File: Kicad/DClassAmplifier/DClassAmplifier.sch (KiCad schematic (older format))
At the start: 9 parts

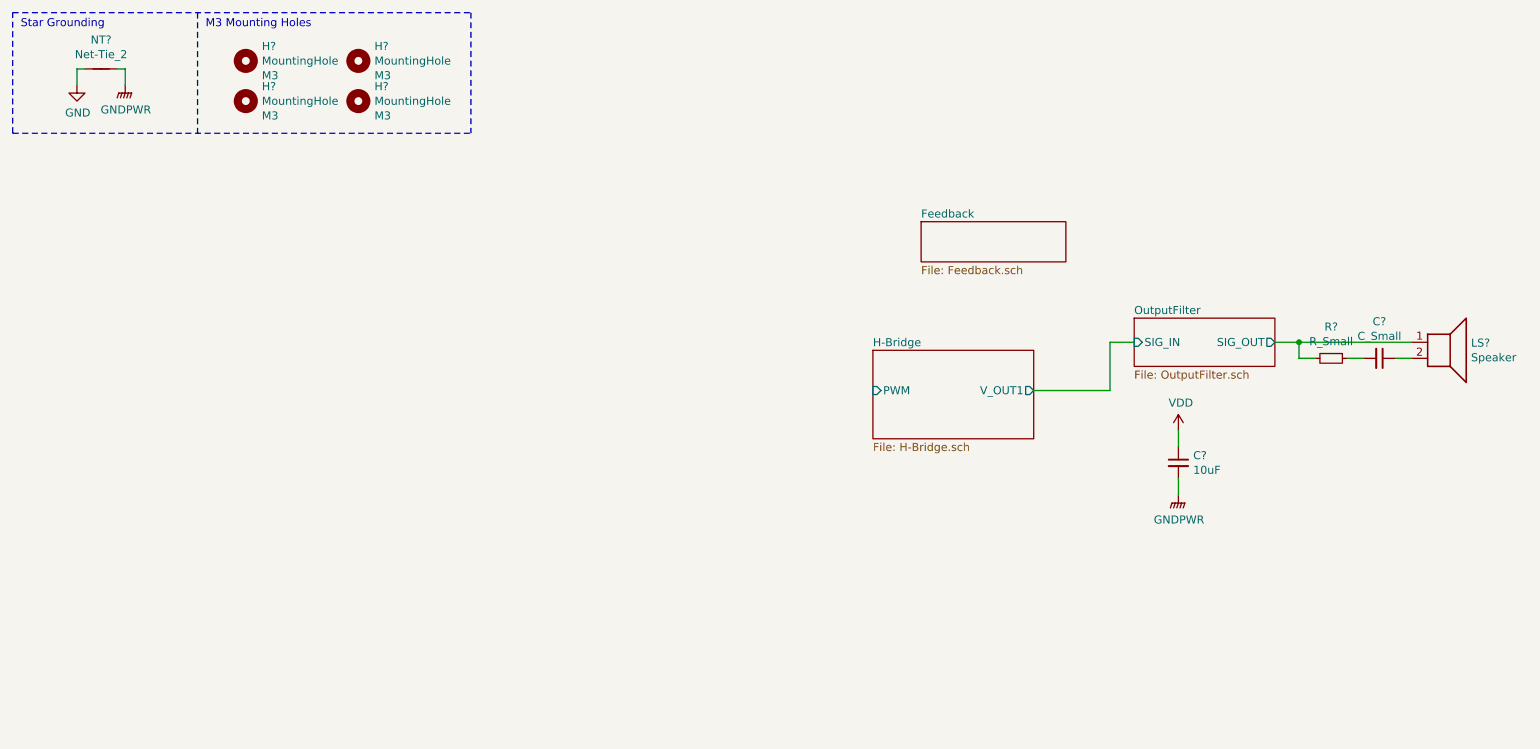
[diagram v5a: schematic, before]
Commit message: Added Dummy Comparator to schematic and duplicated drive.
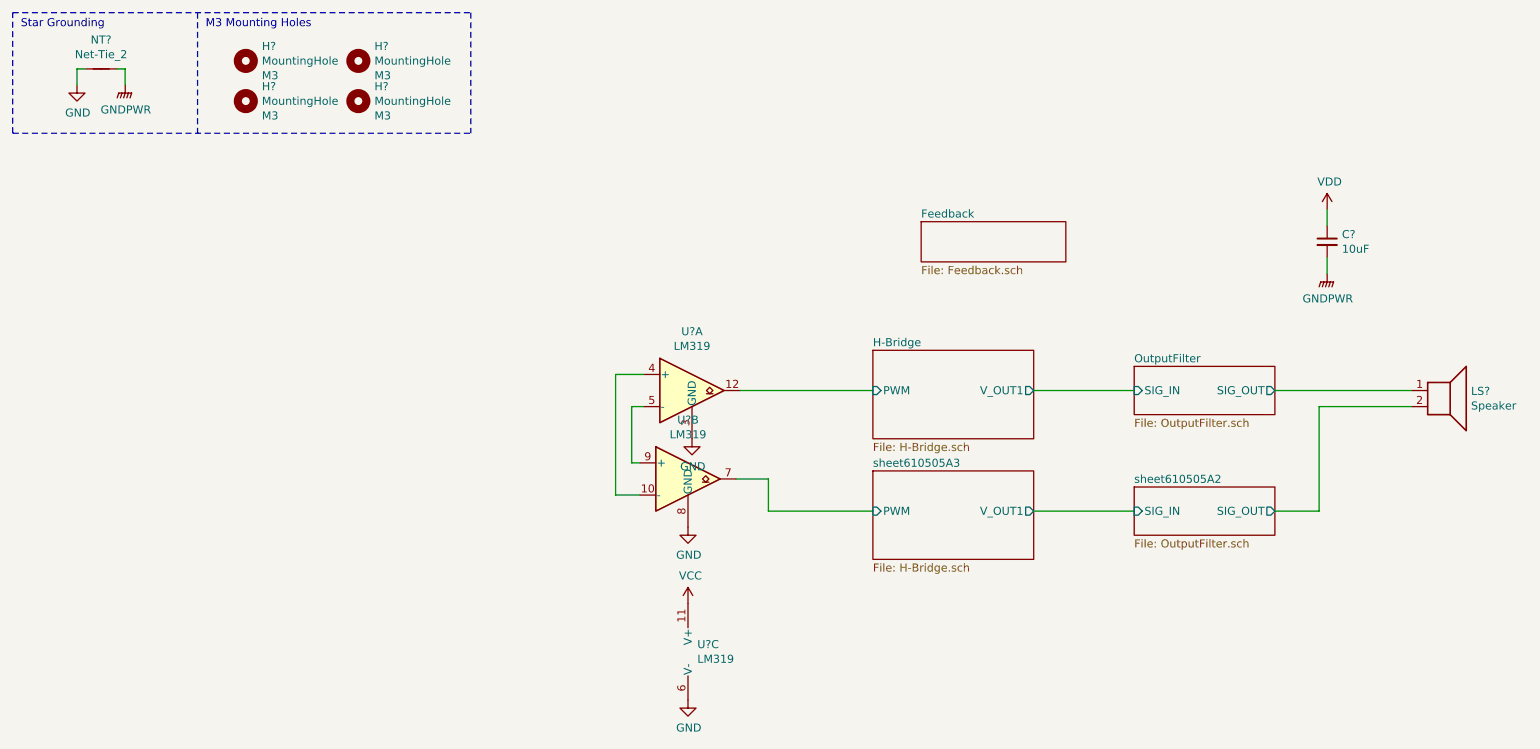
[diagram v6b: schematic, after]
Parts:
- removed C?: C_Small, symbol Device:C_Small
- removed R?: R_Small, symbol Device:R_Small
- added U? (x3): LM319, symbol Comparator:LM319
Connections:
- net GND: now also U?.3 (GND), U?.6 (V-), U?.8 (GND)
- net H-Bridge/PWM: now also U?.12
- net sheet610505A2/SIG_OUT: now reaches LS?.2
- new net: U?.10 (-), U?.4 (+)
- new net: U?.5 (-), U?.9 (+)
- new net VCC: U?.11 (V+)
- new net sheet610505A3/PWM: U?.7
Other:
- moved on the sheet: C?, LS?
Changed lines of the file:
@@
 $Descr A4 11693 8268
 encoding utf-8
-Sheet 1 4
+Sheet 1 6
 Title ""
 Date ""
@@
 $EndDescr
 $Sheet
-S 7625 2500 875  300
+S 7625 2800 875  300
 U 60F78807
 F0 "OutputFilter" 50
 F1 "OutputFilter.sch" 50
-F2 "SIG_IN" I L 7625 2650 50
-F3 "SIG_OUT" O R 8500 2650 50
+F2 "SIG_IN" I L 7625 2950 50
+F3 "SIG_OUT" O R 8500 2950 50
 $EndSheet
 $Comp
@@
 L Device:Speaker LS?
 U 1 1 60FD7EA0
-P 9550 2650
-F 0 "LS?" H 9720 2646 50  0000 L CNN
-F 1 "Speaker" H 9720 2555 50  0000 L CNN
-F 2 "" H 9550 2450 50  0001 C CNN
-F 3 "~" H 9540 2600 50  0001 C CNN
-	1    9550 2650
-	1    0    0    -1
-$EndComp
-Wire Wire Line
-	9350 2650 8650 2650
-$Comp
-L Device:R_Small R?
-U 1 1 60FD8CE8
-P 8850 2750
-F 0 "R?" V 8654 2750 50  0000 C CNN
-F 1 "R_Small" V 8745 2750 50  0000 C CNN
-F 2 "" H 8850 2750 50  0001 C CNN
-F 3 "~" H 8850 2750 50  0001 C CNN
-	1    8850 2750
-	0    1    1    0
-$EndComp
-$Comp
-L Device:C_Small C?
-U 1 1 60FD982C
-P 9150 2750
-F 0 "C?" V 8921 2750 50  0000 C CNN
-F 1 "C_Small" V 9012 2750 50  0000 C CNN
-F 2 "" H 9150 2750 50  0001 C CNN
-F 3 "~" H 9150 2750 50  0001 C CNN
-	1    9150 2750
-	0    1    1    0
-$EndComp
-Wire Wire Line
-	9250 2750 9350 2750
-Wire Wire Line
-	9050 2750 8950 2750
-Wire Wire Line
-	8750 2750 8650 2750
-Wire Wire Line
-	8650 2750 8650 2650
-Connection ~ 8650 2650
-Wire Wire Line
-	8650 2650 8500 2650
+P 9550 2950
+F 0 "LS?" H 9720 2946 50  0000 L CNN
+F 1 "Speaker" H 9720 2855 50  0000 L CNN
+F 2 "" H 9550 2750 50  0001 C CNN
+F 3 "~" H 9540 2900 50  0001 C CNN
+	1    9550 2950
+	1    0    0    -1
+$EndComp
 $Sheet
 S 6300 1900 900  250
@@
 Text Notes 1850 700  0    50   ~ 0
 M3 Mounting Holes
-Wire Wire Line
-	7625 2650 7475 2650
-Wire Wire Line
-	7475 2650 7475 2950
-Wire Wire Line
-	7475 2950 7000 2950
 $Comp
 L power:VDD #PWR?
 U 1 1 6101A943
-P 7900 3200
-F 0 "#PWR?" H 7900 3050 50  0001 C CNN
-F 1 "VDD" H 7915 3373 50  0000 C CNN
-F 2 "" H 7900 3200 50  0001 C CNN
-F 3 "" H 7900 3200 50  0001 C CNN
-	1    7900 3200
+P 8825 1825
+F 0 "#PWR?" H 8825 1675 50  0001 C CNN
+F 1 "VDD" H 8840 1998 50  0000 C CNN
+F 2 "" H 8825 1825 50  0001 C CNN
+F 3 "" H 8825 1825 50  0001 C CNN
+	1    8825 1825
 	1    0    0    -1
 $EndComp
@@
 L power:GNDPWR #PWR?
 U 1 1 6101A949
-P 7900 3600
-F 0 "#PWR?" H 7900 3400 50  0001 C CNN
-F 1 "GNDPWR" H 7904 3446 50  0000 C CNN
-F 2 "" H 7900 3550 50  0001 C CNN
-F 3 "" H 7900 3550 50  0001 C CNN
-	1    7900 3600
+P 8825 2225
+F 0 "#PWR?" H 8825 2025 50  0001 C CNN
+F 1 "GNDPWR" H 8829 2071 50  0000 C CNN
+F 2 "" H 8825 2175 50  0001 C CNN
+F 3 "" H 8825 2175 50  0001 C CNN
+	1    8825 2225
 	1    0    0    -1
 $EndComp
@@
 L Device:C_Small C?
 U 1 1 6101A94F
-P 7900 3400
+P 8825 2025
 AR Path="/60FDBB90/6101A94F" Ref="C?"  Part="1"
 AR Path="/6101A94F" Ref="C?"  Part="1"
-F 0 "C?" H 7992 3446 50  0000 L CNN
-F 1 "10uF" H 7992 3355 50  0000 L CNN
-F 2 "" H 7900 3400 50  0001 C CNN
-F 3 "~" H 7900 3400 50  0001 C CNN
-	1    7900 3400
-	1    0    0    -1
-$EndComp
-Wire Wire Line
-	7900 3600 7900 3500
-Wire Wire Line
-	7900 3200 7900 3300
+F 0 "C?" H 8917 2071 50  0000 L CNN
+F 1 "10uF" H 8917 1980 50  0000 L CNN
+F 2 "" H 8825 2025 50  0001 C CNN
+F 3 "~" H 8825 2025 50  0001 C CNN
+	1    8825 2025
+	1    0    0    -1
+$EndComp
+Wire Wire Line
+	8825 2225 8825 2125
+Wire Wire Line
+	8825 1825 8825 1925
+$Comp
+L Comparator:LM319 U?
+U 1 1 6103E3C3
+P 4875 2950
+F 0 "U?" H 4875 3317 50  0000 C CNN
+F 1 "LM319" H 4875 3226 50  0000 C CNN
+F 2 "" H 4875 2950 50  0001 C CNN
+F 3 "http://www.ti.com/lit/ds/symlink/lm319-n.pdf" H 4875 2950 50  0001 C CNN
+	1    4875 2950
+	1    0    0    -1
+$EndComp
+$Comp
+L Comparator:LM319 U?
+U 2 1 6103EEF0
+P 4850 3500
+F 0 "U?" H 4850 3867 50  0000 C CNN
+F 1 "LM319" H 4850 3776 50  0000 C CNN
+F 2 "" H 4850 3500 50  0001 C CNN
+F 3 "http://www.ti.com/lit/ds/symlink/lm319-n.pdf" H 4850 3500 50  0001 C CNN
+	2    4850 3500
+	1    0    0    -1
+$EndComp
+$Comp
+L Comparator:LM319 U?
+U 3 1 6103FBAA
+P 4950 4575
+F 0 "U?" H 4908 4621 50  0000 L CNN
+F 1 "LM319" H 4908 4530 50  0000 L CNN
+F 2 "" H 4950 4575 50  0001 C CNN
+F 3 "http://www.ti.com/lit/ds/symlink/lm319-n.pdf" H 4950 4575 50  0001 C CNN
+	3    4950 4575
+	1    0    0    -1
+$EndComp
+Wire Wire Line
+	6000 2950 5175 2950
+Wire Wire Line
+	8500 2950 9350 2950
+Wire Wire Line
+	7000 2950 7625 2950
+$Sheet
+S 7625 3550 875  300
+U 610505A7
+F0 "sheet610505A2" 50
+F1 "OutputFilter.sch" 50
+F2 "SIG_IN" I L 7625 3700 50
+F3 "SIG_OUT" O R 8500 3700 50
+$EndSheet
+$Sheet
+S 6000 3450 1000 550
+U 610505AB
+F0 "sheet610505A3" 50
+F1 "H-Bridge.sch" 50
+F2 "PWM" I L 6000 3700 50
+F3 "V_OUT1" O R 7000 3700 50
+$EndSheet
+Wire Wire Line
+	7000 3700 7625 3700
+Wire Wire Line
+	8500 3700 8775 3700
+Wire Wire Line
+	8775 3700 8775 3050
+Wire Wire Line
+	8775 3050 9350 3050
+Wire Wire Line
+	6000 3700 5350 3700
+Wire Wire Line
+	5350 3700 5350 3500
+Wire Wire Line
+	5350 3500 5150 3500
+Wire Wire Line
+	4575 3050 4500 3050
+Wire Wire Line
+	4500 3050 4500 3400
+Wire Wire Line
+	4500 3400 4550 3400
+Wire Wire Line
+	4575 2850 4400 2850
+Wire Wire Line
+	4400 2850 4400 3600
+Wire Wire Line
+	4400 3600 4550 3600
+$Comp
+L power:GND #PWR?
+U 1 1 61053271
+P 4875 3250
+F 0 "#PWR?" H 4875 3000 50  0001 C CNN
+F 1 "GND" H 4880 3077 50  0000 C CNN
+F 2 "" H 4875 3250 50  0001 C CNN
+F 3 "" H 4875 3250 50  0001 C CNN
+	1    4875 3250
+	1    0    0    -1
+$EndComp
+$Comp
+L power:GND #PWR?
+U 1 1 61053814
+P 4850 3800
+F 0 "#PWR?" H 4850 3550 50  0001 C CNN
+F 1 "GND" H 4855 3627 50  0000 C CNN
+F 2 "" H 4850 3800 50  0001 C CNN
+F 3 "" H 4850 3800 50  0001 C CNN
+	1    4850 3800
+	1    0    0    -1
+$EndComp
+$Comp
+L power:GND #PWR?
+U 1 1 61054142
+P 4850 4875
+F 0 "#PWR?" H 4850 4625 50  0001 C CNN
+F 1 "GND" H 4855 4702 50  0000 C CNN
+F 2 "" H 4850 4875 50  0001 C CNN
+F 3 "" H 4850 4875 50  0001 C CNN
+	1    4850 4875
+	1    0    0    -1
+$EndComp
+$Comp
+L power:VCC #PWR?
+U 1 1 6105AFC3
+P 4850 4275
+F 0 "#PWR?" H 4850 4125 50  0001 C CNN
+F 1 "VCC" H 4865 4448 50  0000 C CNN
+F 2 "" H 4850 4275 50  0001 C CNN
+F 3 "" H 4850 4275 50  0001 C CNN
+	1    4850 4275
+	1    0    0    -1
+$EndComp
 $EndSCHEMATC

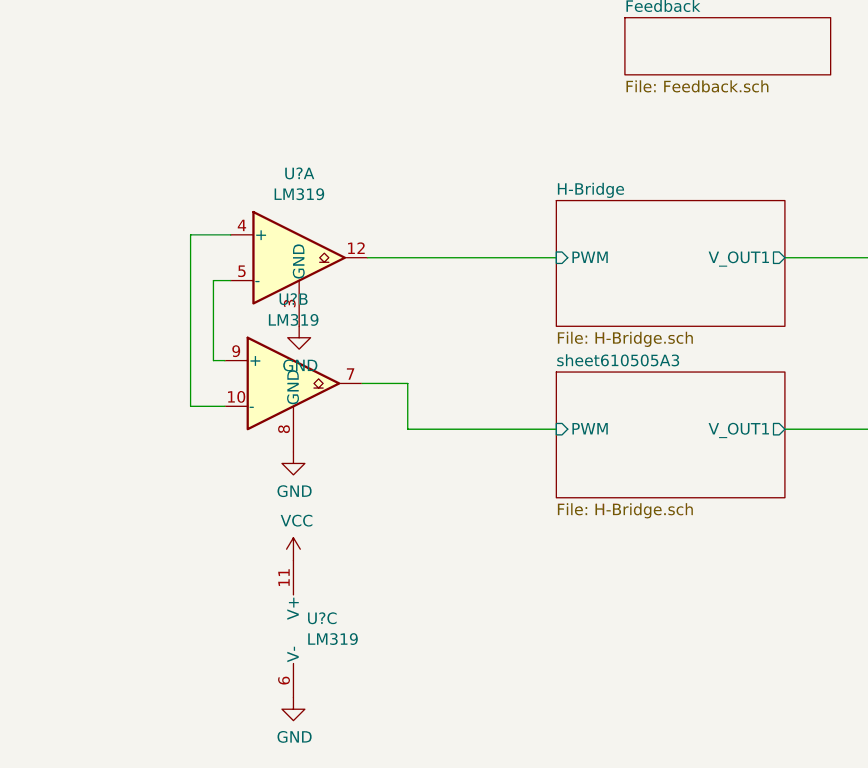
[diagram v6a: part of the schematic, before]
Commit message: Hierarchical Comparator Sheet
Updated Gate Driver as well
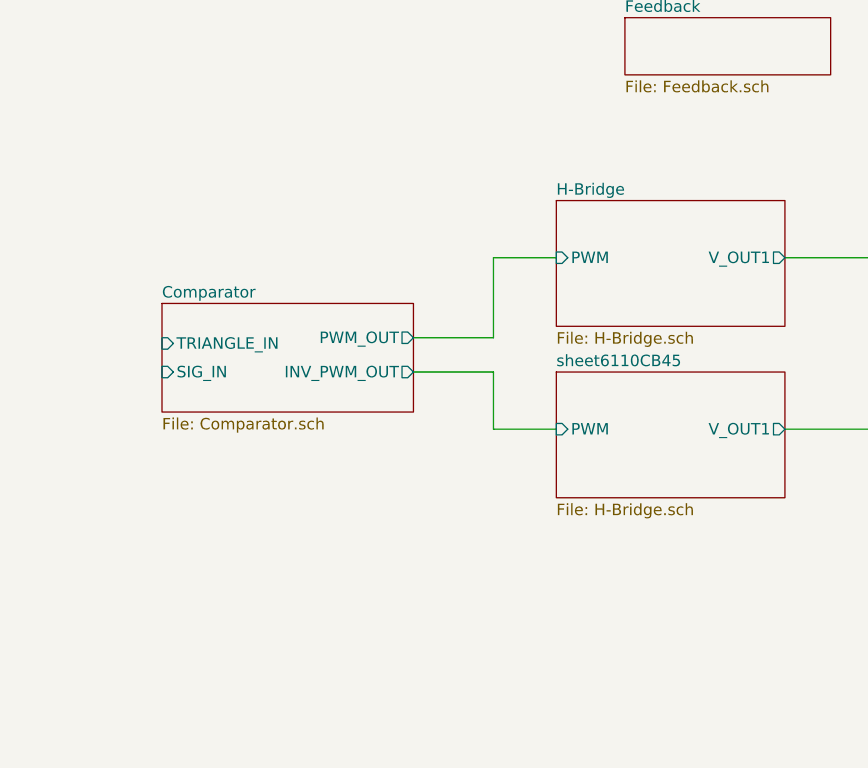
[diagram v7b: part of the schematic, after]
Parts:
- removed U? (x3): LM319, symbol Comparator:LM319
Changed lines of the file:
@@
 $Descr A4 11693 8268
 encoding utf-8
-Sheet 1 6
+Sheet 1 7
 Title ""
 Date ""
@@
 Wire Wire Line
 	8825 1825 8825 1925
-$Comp
-L Comparator:LM319 U?
-U 1 1 6103E3C3
-P 4875 2950
-F 0 "U?" H 4875 3317 50  0000 C CNN
-F 1 "LM319" H 4875 3226 50  0000 C CNN
-F 2 "" H 4875 2950 50  0001 C CNN
-F 3 "http://www.ti.com/lit/ds/symlink/lm319-n.pdf" H 4875 2950 50  0001 C CNN
-	1    4875 2950
-	1    0    0    -1
-$EndComp
-$Comp
-L Comparator:LM319 U?
-U 2 1 6103EEF0
-P 4850 3500
-F 0 "U?" H 4850 3867 50  0000 C CNN
-F 1 "LM319" H 4850 3776 50  0000 C CNN
-F 2 "" H 4850 3500 50  0001 C CNN
-F 3 "http://www.ti.com/lit/ds/symlink/lm319-n.pdf" H 4850 3500 50  0001 C CNN
-	2    4850 3500
-	1    0    0    -1
-$EndComp
-$Comp
-L Comparator:LM319 U?
-U 3 1 6103FBAA
-P 4950 4575
-F 0 "U?" H 4908 4621 50  0000 L CNN
-F 1 "LM319" H 4908 4530 50  0000 L CNN
-F 2 "" H 4950 4575 50  0001 C CNN
-F 3 "http://www.ti.com/lit/ds/symlink/lm319-n.pdf" H 4950 4575 50  0001 C CNN
-	3    4950 4575
-	1    0    0    -1
-$EndComp
-Wire Wire Line
-	6000 2950 5175 2950
 Wire Wire Line
 	8500 2950 9350 2950
@@
 F3 "SIG_OUT" O R 8500 3700 50
 $EndSheet
+Wire Wire Line
+	7000 3700 7625 3700
+Wire Wire Line
+	8500 3700 8775 3700
+Wire Wire Line
+	8775 3700 8775 3050
+Wire Wire Line
+	8775 3050 9350 3050
 $Sheet
 S 6000 3450 1000 550
-U 610505AB
-F0 "sheet610505A3" 50
+U 6110CB49
+F0 "sheet6110CB45" 50
 F1 "H-Bridge.sch" 50
 F2 "PWM" I L 6000 3700 50
 F3 "V_OUT1" O R 7000 3700 50
 $EndSheet
-Wire Wire Line
-	7000 3700 7625 3700
-Wire Wire Line
-	8500 3700 8775 3700
-Wire Wire Line
-	8775 3700 8775 3050
-Wire Wire Line
-	8775 3050 9350 3050
-Wire Wire Line
-	6000 3700 5350 3700
-Wire Wire Line
-	5350 3700 5350 3500
-Wire Wire Line
-	5350 3500 5150 3500
-Wire Wire Line
-	4575 3050 4500 3050
-Wire Wire Line
-	4500 3050 4500 3400
-Wire Wire Line
-	4500 3400 4550 3400
-Wire Wire Line
-	4575 2850 4400 2850
-Wire Wire Line
-	4400 2850 4400 3600
-Wire Wire Line
-	4400 3600 4550 3600
-$Comp
-L power:GND #PWR?
-U 1 1 61053271
-P 4875 3250
-F 0 "#PWR?" H 4875 3000 50  0001 C CNN
-F 1 "GND" H 4880 3077 50  0000 C CNN
-F 2 "" H 4875 3250 50  0001 C CNN
-F 3 "" H 4875 3250 50  0001 C CNN
-	1    4875 3250
-	1    0    0    -1
-$EndComp
-$Comp
-L power:GND #PWR?
-U 1 1 61053814
-P 4850 3800
-F 0 "#PWR?" H 4850 3550 50  0001 C CNN
-F 1 "GND" H 4855 3627 50  0000 C CNN
-F 2 "" H 4850 3800 50  0001 C CNN
-F 3 "" H 4850 3800 50  0001 C CNN
-	1    4850 3800
-	1    0    0    -1
-$EndComp
-$Comp
-L power:GND #PWR?
-U 1 1 61054142
-P 4850 4875
-F 0 "#PWR?" H 4850 4625 50  0001 C CNN
-F 1 "GND" H 4855 4702 50  0000 C CNN
-F 2 "" H 4850 4875 50  0001 C CNN
-F 3 "" H 4850 4875 50  0001 C CNN
-	1    4850 4875
-	1    0    0    -1
-$EndComp
-$Comp
-L power:VCC #PWR?
-U 1 1 6105AFC3
-P 4850 4275
-F 0 "#PWR?" H 4850 4125 50  0001 C CNN
-F 1 "VCC" H 4865 4448 50  0000 C CNN
-F 2 "" H 4850 4275 50  0001 C CNN
-F 3 "" H 4850 4275 50  0001 C CNN
-	1    4850 4275
-	1    0    0    -1
-$EndComp
+$Sheet
+S 4275 3150 1100 475
+U 61113C55
+F0 "Comparator" 50
+F1 "Comparator.sch" 50
+F2 "PWM_OUT" O R 5375 3300 50
+F3 "INV_PWM_OUT" O R 5375 3450 50
+F4 "TRIANGLE_IN" I L 4275 3325 50
+F5 "SIG_IN" I L 4275 3450 50
+$EndSheet
+Wire Wire Line
+	5375 3450 5725 3450
+Wire Wire Line
+	5725 3450 5725 3700
+Wire Wire Line
+	5725 3700 6000 3700
+Wire Wire Line
+	6000 2950 5725 2950
+Wire Wire Line
+	5725 2950 5725 3300
+Wire Wire Line
+	5725 3300 5375 3300
 $EndSCHEMATC

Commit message: Lol Whoops, changes??
Oh it was me moving things around a little bit
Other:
- moved on the sheet: LS?
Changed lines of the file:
@@
 L Device:Speaker LS?
 U 1 1 60FD7EA0
-P 9550 2950
-F 0 "LS?" H 9720 2946 50  0000 L CNN
-F 1 "Speaker" H 9720 2855 50  0000 L CNN
-F 2 "" H 9550 2750 50  0001 C CNN
-F 3 "~" H 9540 2900 50  0001 C CNN
-	1    9550 2950
+P 9550 3250
+F 0 "LS?" H 9720 3246 50  0000 L CNN
+F 1 "Speaker" H 9720 3155 50  0000 L CNN
+F 2 "" H 9550 3050 50  0001 C CNN
+F 3 "~" H 9540 3200 50  0001 C CNN
+	1    9550 3250
 	1    0    0    -1
 $EndComp
@@
 	8825 1825 8825 1925
 Wire Wire Line
-	8500 2950 9350 2950
-Wire Wire Line
 	7000 2950 7625 2950
 $Sheet
@@
 	8500 3700 8775 3700
 Wire Wire Line
-	8775 3700 8775 3050
-Wire Wire Line
-	8775 3050 9350 3050
+	8775 3350 9350 3350
 $Sheet
 S 6000 3450 1000 550
@@
 Wire Wire Line
 	5725 3300 5375 3300
+Wire Wire Line
+	9350 3250 8775 3250
+Wire Wire Line
+	8775 2950 8500 2950
+Wire Wire Line
+	8775 3250 8775 2950
+Wire Wire Line
+	8775 3350 8775 3700
 $EndSCHEMATC
